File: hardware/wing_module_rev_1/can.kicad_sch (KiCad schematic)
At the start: 9 parts, among them J7 Conn_01x04, J8 Conn_01x04, U6 TCAN3403

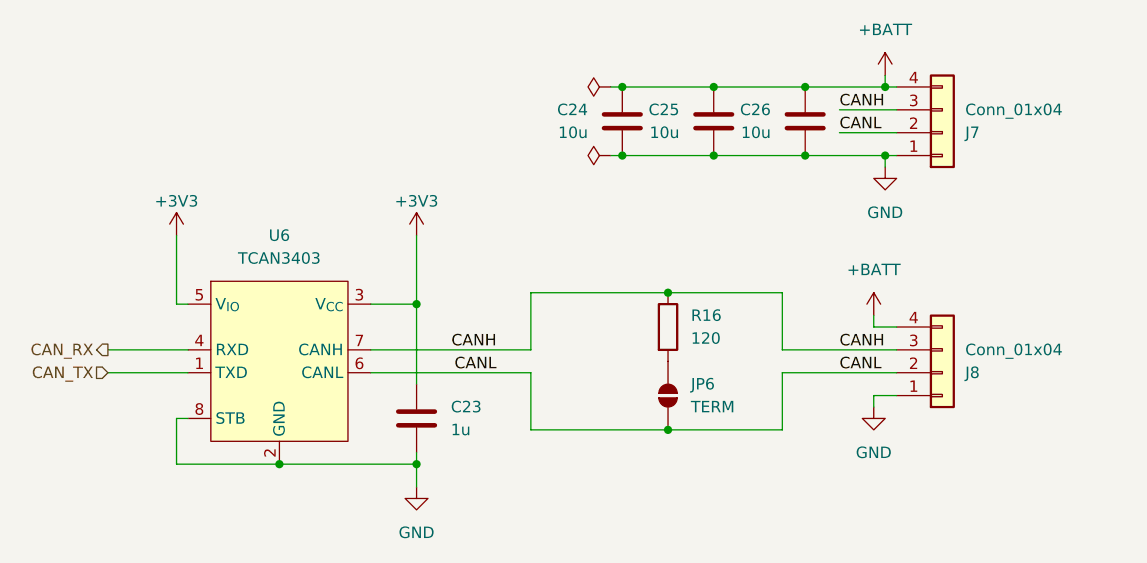
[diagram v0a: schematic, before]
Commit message: Adjusted CAN connector order, drafting floorplan
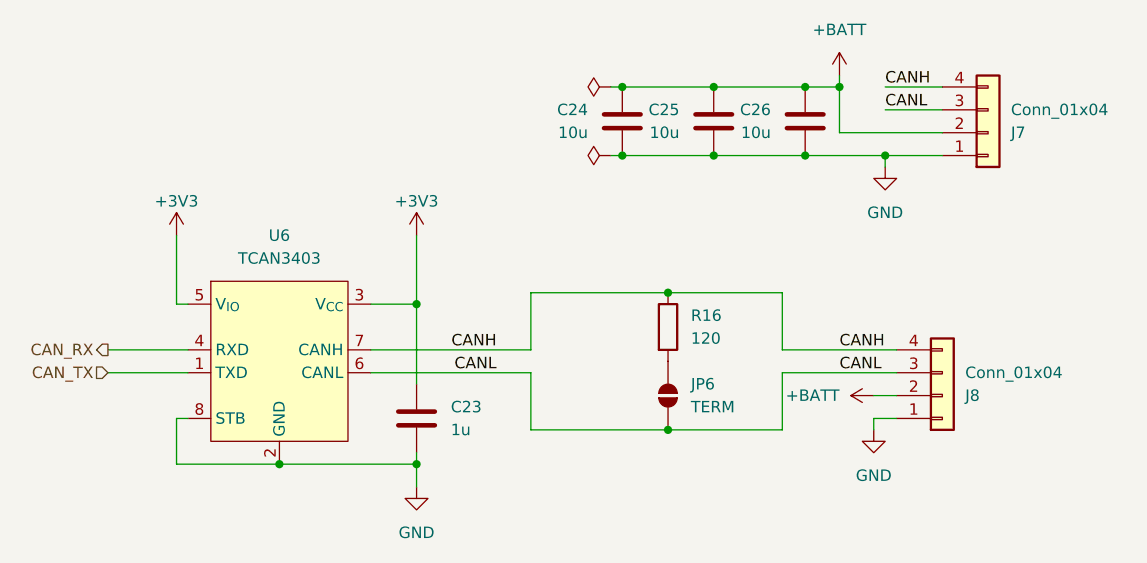
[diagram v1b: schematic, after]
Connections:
- net +BATT: now also J7.2 (Pin_2), J8.2 (Pin_2); no longer J7.4 (Pin_4), J8.4 (Pin_4)
- net CANH: now also J7.4 (Pin_4), J8.4 (Pin_4); no longer J7.3 (Pin_3), J8.3 (Pin_3)
- net CANL: now also J7.3 (Pin_3), J8.3 (Pin_3); no longer J7.2 (Pin_2), J8.2 (Pin_2)
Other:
- moved on the sheet: J7, J8

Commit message: Reassigned reference numbers
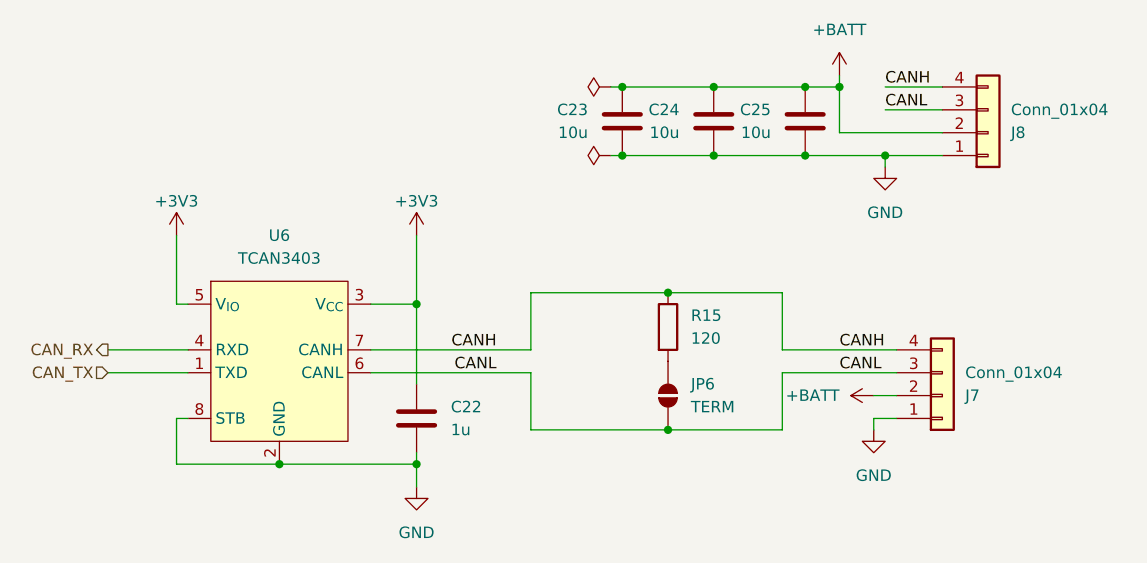
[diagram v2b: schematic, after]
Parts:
- renumbered C23 to C22, C24 to C23, C25 to C24, C26 to C25, J8 to J7, J7 to J8, R16 to R15
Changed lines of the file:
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@@
 		(on_board yes)
 		(dnp no)
-		(property "Reference" "J8"
+		(property "Reference" "J7"
 			(at 193.04 110.4901 0)
 			(effects
@@
 			(project "wing_module_rev_1"
 				(path "/7b7fffa9-e888-4279-94bf-385d74cf78f9/f20f1d55-4513-4ee1-ac5d-1656e10991e6"
-					(reference "J8")
+					(reference "J7")
 					(unit 1)
 				)
@@
 		(on_board yes)
 		(dnp no)
-		(property "Reference" "C24"
+		(property "Reference" "C23"
 			(at 151.13 78.7399 0)
 			(effects
@@
 			(project "wing_module_rev_1"
 				(path "/7b7fffa9-e888-4279-94bf-385d74cf78f9/f20f1d55-4513-4ee1-ac5d-1656e10991e6"
-					(reference "C24")
+					(reference "C23")
 					(unit 1)
 				)
@@
 		(on_board yes)
 		(dnp no)
-		(property "Reference" "C26"
+		(property "Reference" "C25"
 			(at 171.45 78.7399 0)
 			(effects
@@
 			(project "wing_module_rev_1"
 				(path "/7b7fffa9-e888-4279-94bf-385d74cf78f9/f20f1d55-4513-4ee1-ac5d-1656e10991e6"
-					(reference "C26")
+					(reference "C25")
 					(unit 1)
 				)
@@
 		(on_board yes)
 		(dnp no)
-		(property "Reference" "C25"
+		(property "Reference" "C24"
 			(at 161.29 78.7399 0)
 			(effects
@@
 			(project "wing_module_rev_1"
 				(path "/7b7fffa9-e888-4279-94bf-385d74cf78f9/f20f1d55-4513-4ee1-ac5d-1656e10991e6"
-					(reference "C25")
+					(reference "C24")
 					(unit 1)
 				)
@@
 		(dnp no)
 		(fields_autoplaced yes)
-		(property "Reference" "C23"
+		(property "Reference" "C22"
 			(at 135.89 111.7599 0)
 			(effects
@@
 			(project "wing_module_rev_1"
 				(path "/7b7fffa9-e888-4279-94bf-385d74cf78f9/f20f1d55-4513-4ee1-ac5d-1656e10991e6"
-					(reference "C23")
+					(reference "C22")
 					(unit 1)
 				)
@@
 		(dnp no)
 		(fields_autoplaced yes)
-		(property "Reference" "#PWR048"
+		(property "Reference" "#PWR047"
 			(at 132.08 127 0)
 			(effects
@@
 			(project "wing_module_rev_1"
 				(path "/7b7fffa9-e888-4279-94bf-385d74cf78f9/f20f1d55-4513-4ee1-ac5d-1656e10991e6"
-					(reference "#PWR048")
+					(reference "#PWR047")
 					(unit 1)
 				)
@@
 		(on_board yes)
 		(dnp no)
-		(property "Reference" "#PWR046"
+		(property "Reference" "#PWR045"
 			(at 105.41 96.52 0)
 			(effects
@@
 			(project "wing_module_rev_1"
 				(path "/7b7fffa9-e888-4279-94bf-385d74cf78f9/f20f1d55-4513-4ee1-ac5d-1656e10991e6"
-					(reference "#PWR046")
+					(reference "#PWR045")
 					(unit 1)
 				)
@@
 		(dnp no)
 		(fields_autoplaced yes)
-		(property "Reference" "R16"
+		(property "Reference" "R15"
 			(at 162.56 101.5999 0)
 			(effects
@@
 			(project "wing_module_rev_1"
 				(path "/7b7fffa9-e888-4279-94bf-385d74cf78f9/f20f1d55-4513-4ee1-ac5d-1656e10991e6"
-					(reference "R16")
+					(reference "R15")
 					(unit 1)
 				)
@@
 		(on_board yes)
 		(dnp no)
-		(property "Reference" "J7"
+		(property "Reference" "J8"
 			(at 198.12 81.2801 0)
 			(effects
@@
 			(project "wing_module_rev_1"
 				(path "/7b7fffa9-e888-4279-94bf-385d74cf78f9/f20f1d55-4513-4ee1-ac5d-1656e10991e6"
-					(reference "J7")
+					(reference "J8")
 					(unit 1)
 				)
@@
 		(on_board yes)
 		(dnp no)
-		(property "Reference" "#PWR047"
+		(property "Reference" "#PWR046"
 			(at 132.08 96.52 0)
 			(effects
@@
 			(project "wing_module_rev_1"
 				(path "/7b7fffa9-e888-4279-94bf-385d74cf78f9/f20f1d55-4513-4ee1-ac5d-1656e10991e6"
-					(reference "#PWR047")
+					(reference "#PWR046")
 					(unit 1)
 				)
@@
 		(dnp no)
 		(fields_autoplaced yes)
-		(property "Reference" "#PWR051"
+		(property "Reference" "#PWR048"
 			(at 179.07 78.74 0)
 			(effects
@@
 			(project "wing_module_rev_1"
 				(path "/7b7fffa9-e888-4279-94bf-385d74cf78f9/f20f1d55-4513-4ee1-ac5d-1656e10991e6"
-					(reference "#PWR051")
+					(reference "#PWR048")
 					(unit 1)
 				)
@@
 		(dnp no)
 		(fields_autoplaced yes)
-		(property "Reference" "#PWR052"
+		(property "Reference" "#PWR051"
 			(at 184.15 91.44 0)
 			(effects
@@
 			(project "wing_module_rev_1"
 				(path "/7b7fffa9-e888-4279-94bf-385d74cf78f9/f20f1d55-4513-4ee1-ac5d-1656e10991e6"
-					(reference "#PWR052")
-					(unit 1)
-				)
+					(reference "#PWR051")
+					(unit 1)
+				)
